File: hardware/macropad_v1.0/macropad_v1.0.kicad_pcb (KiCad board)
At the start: 2 copper layers, 66.7 x 81 mm, 51 parts, among them J1 USB_C_Receptacle_USB2.0_14P, SW1 SW_Push, SW2 Rotary Encoder, SW3 Rotary Encoder, U1 USBLC6-2SC6, U2 STM32F072C8T6, U3 XC6206PxxxMR

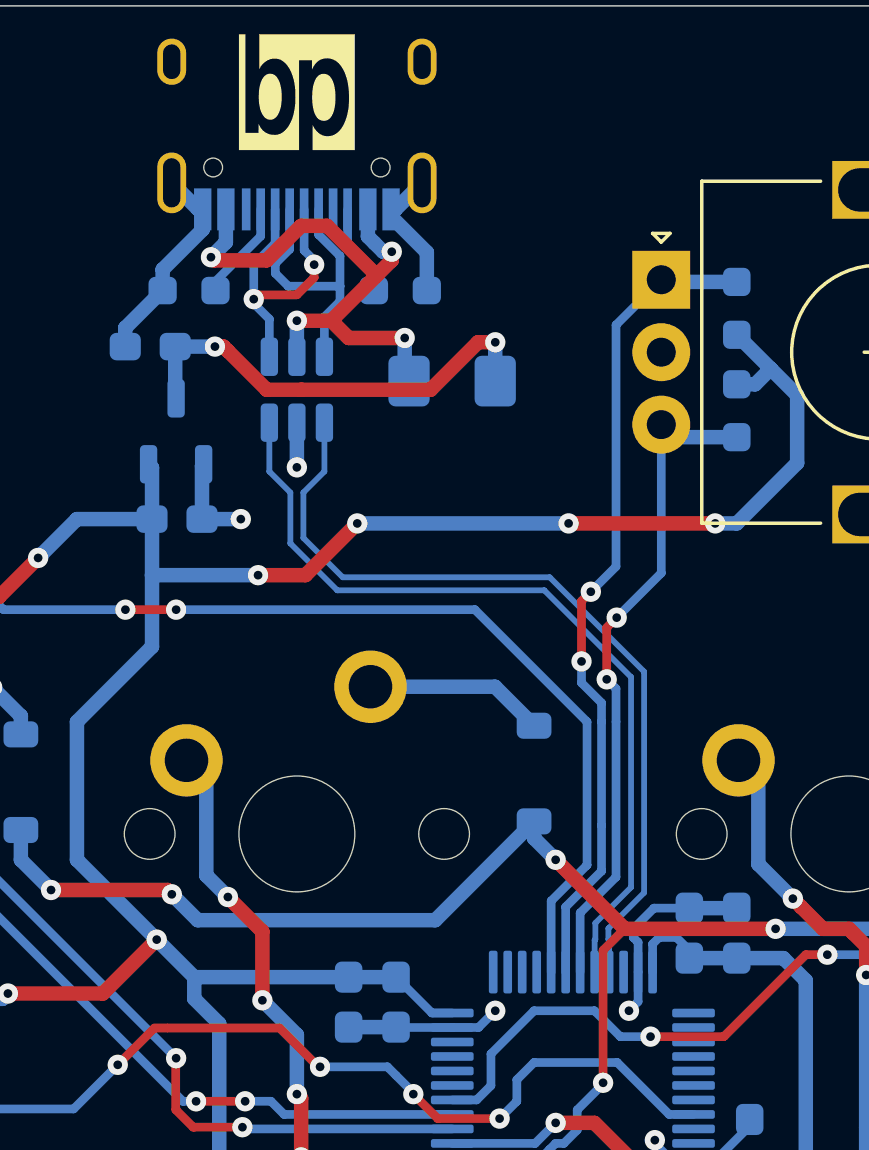
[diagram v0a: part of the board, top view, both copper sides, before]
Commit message: Changed USB-C routing
-Changed routing from usb-c module to esd protection module by shorting the pair of D+ and D- pins. New routing doesn't use a via, has shorter traces from usb module to esd module, and matches the length of the traces for D+ and D- better than the previous design did.

-Increased the width of the differential pair data traces from esd module to mcu from 0.2mm to 0.3mm to match traces that go into the esd module. Kicad made them 0.2mm by default for some reason.

-Next steps: change the routing near the MCU to eliminate overuse of vias, add a ground plane to the bottom layer and add stitching vias to connect the two planes
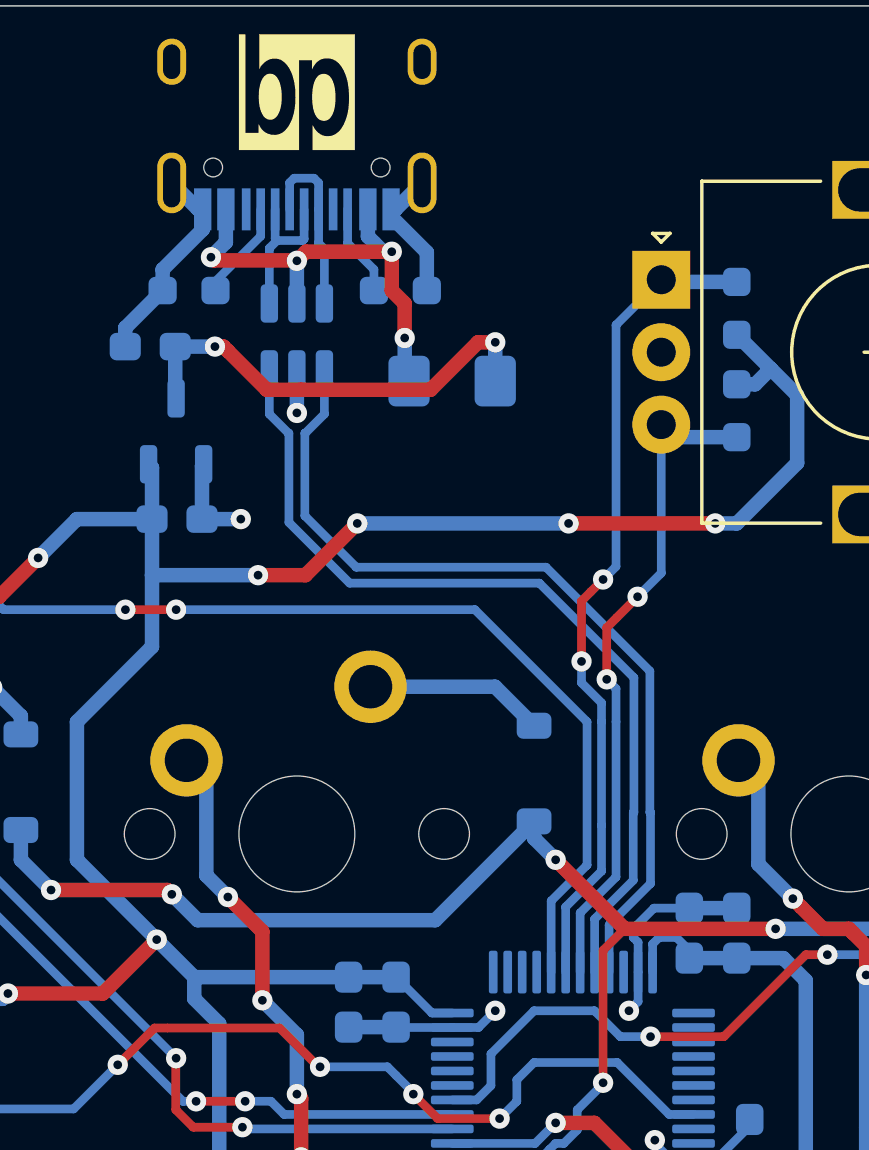
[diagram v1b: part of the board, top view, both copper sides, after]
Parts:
- moved U1 1.84 mm to (200.0, 30.5)
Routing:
- net ESD_D-: track 10.5 -> 5.37 mm, vias 2 -> 0
- net VBUS: track 20.8 -> 16.4 mm
- net ESD_D+: track 10.4 -> 6.30 mm
- net USB_D+: track 28.8 -> 30.5 mm
- net USB_D-: track 28.8 -> 30.4 mm

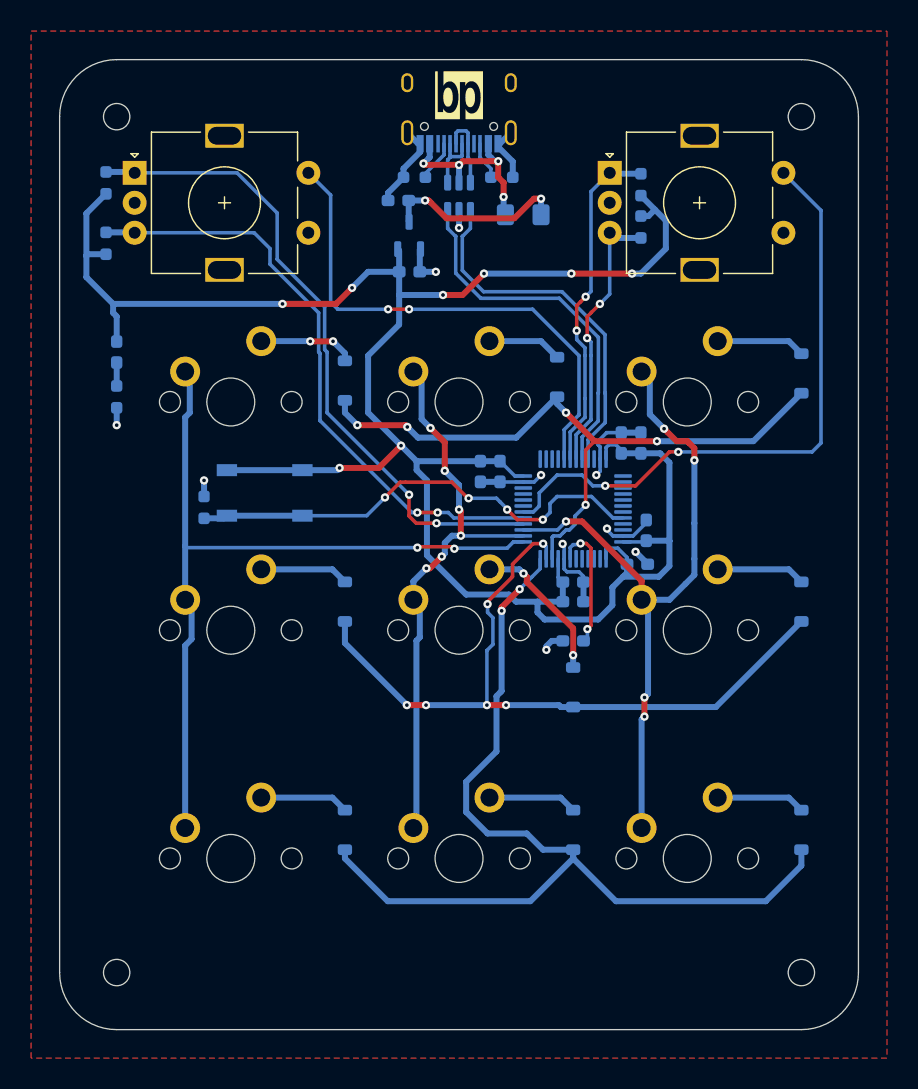
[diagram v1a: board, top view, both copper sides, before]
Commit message: Changed routing
-Edited traces to avoid overusing vias

-Next steps: Add stitching vias to connect the two ground planes
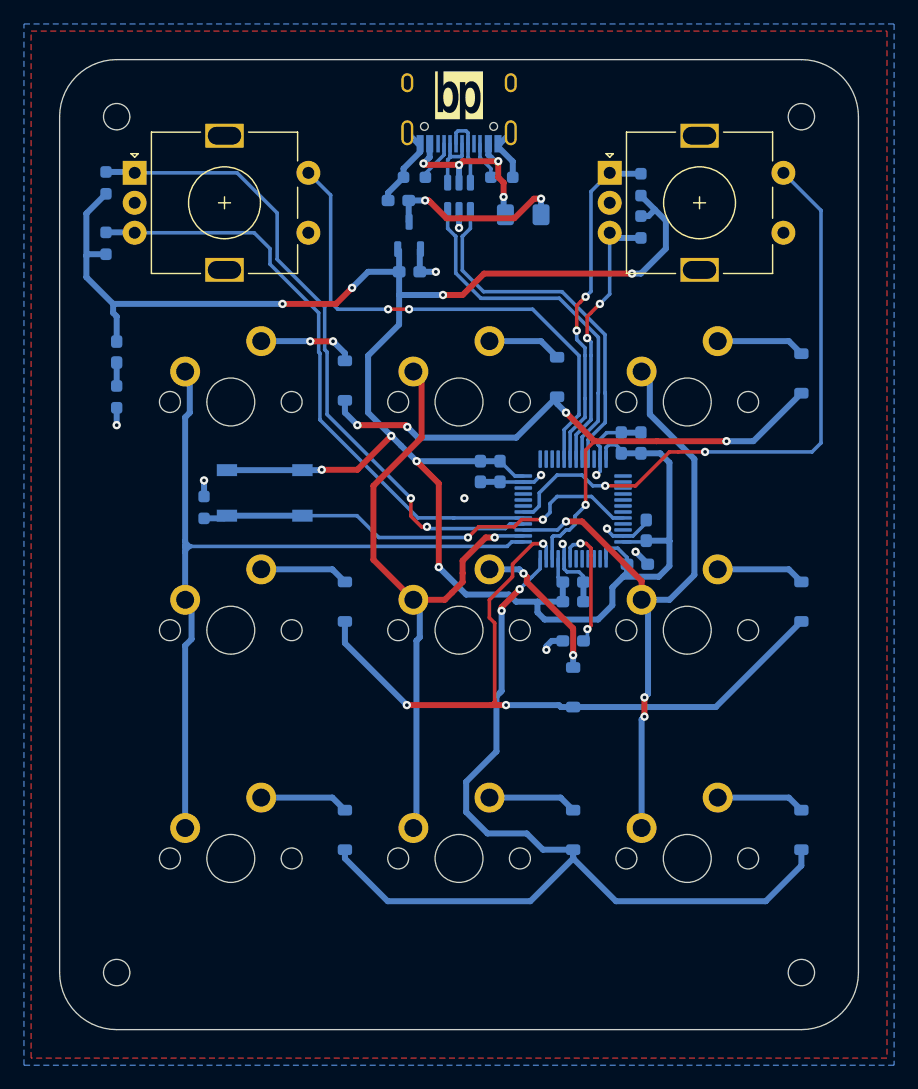
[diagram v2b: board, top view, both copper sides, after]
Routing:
- net COL_1: track 47.7 -> 54.3 mm, vias 6 -> 1
- net COL_0: track 67.5 -> 68.7 mm, vias 2 -> 0
- net BOOT0: track 39.5 -> 38.4 mm, vias 4 -> 2
- net ROW_1: track 62.7 -> 63.5 mm, vias 6 -> 3
- net COL_2: track 57.9 -> 57.4 mm, vias 5 -> 3
- net RENC_B1: track 50.7 -> 50.6 mm, vias 2 -> 0
- net GND: vias 10 -> 11
- added copper zone on B.Cu, net GND

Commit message: Added stitching vias
-Next steps: upload files to jlcpcb, generate a bom, figure out what I'm going to hand-solder, and order everything
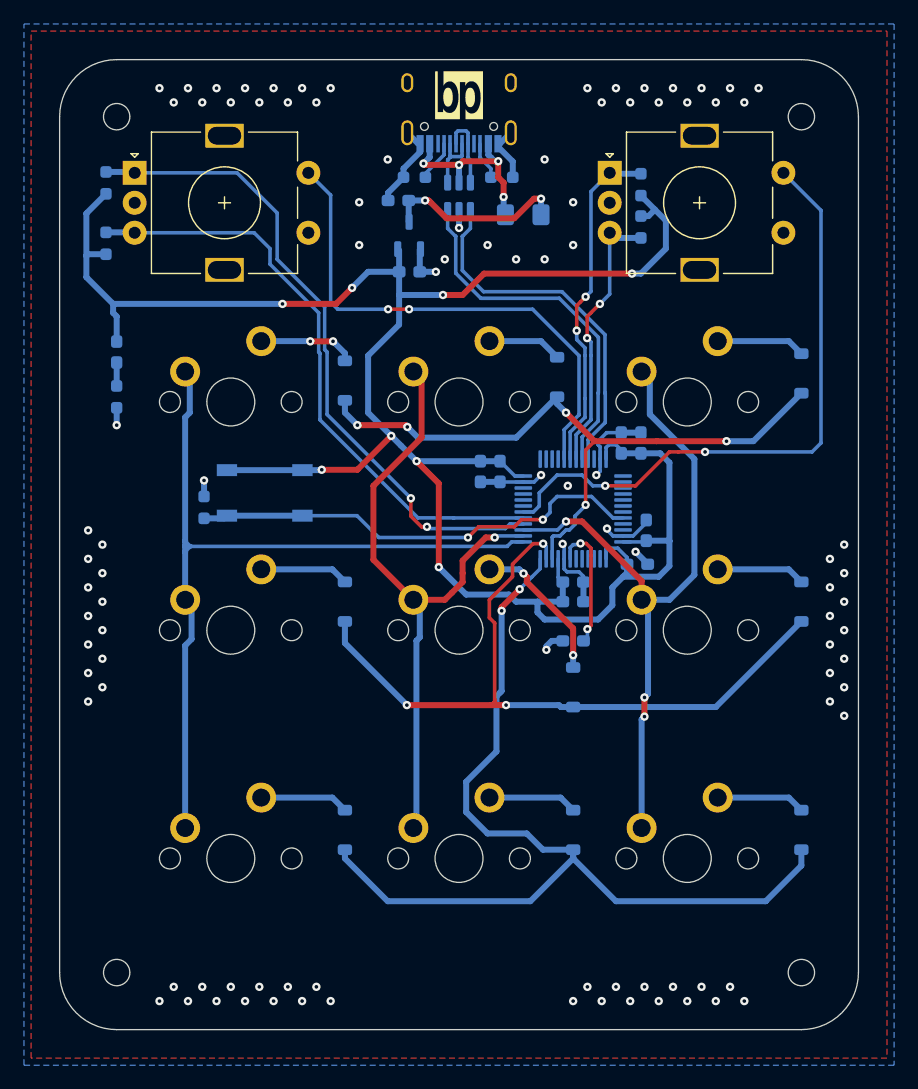
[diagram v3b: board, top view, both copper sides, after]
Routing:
- net GND: vias 11 -> 99

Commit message: Updated silkscreen and naming stuff, added keepouts
-Added ParPad logo to fron silkscreen

-Changed the name of the design in the little design box in the bottom right of the pcb and schematic

-Added two keepout zones to certain areas of the bottom ground fill to avoid an error about thermal spokes (only had one spoke, just got rid of the spoke cuz the top ground layer already has four spokes), and also a warning about some copper thing being too narrow
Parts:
- added G***: LOGO, LOGO, F.Cu at (200.0, 96.4)
- G***: moved to B.Cu
- turned G*** to 180 degrees

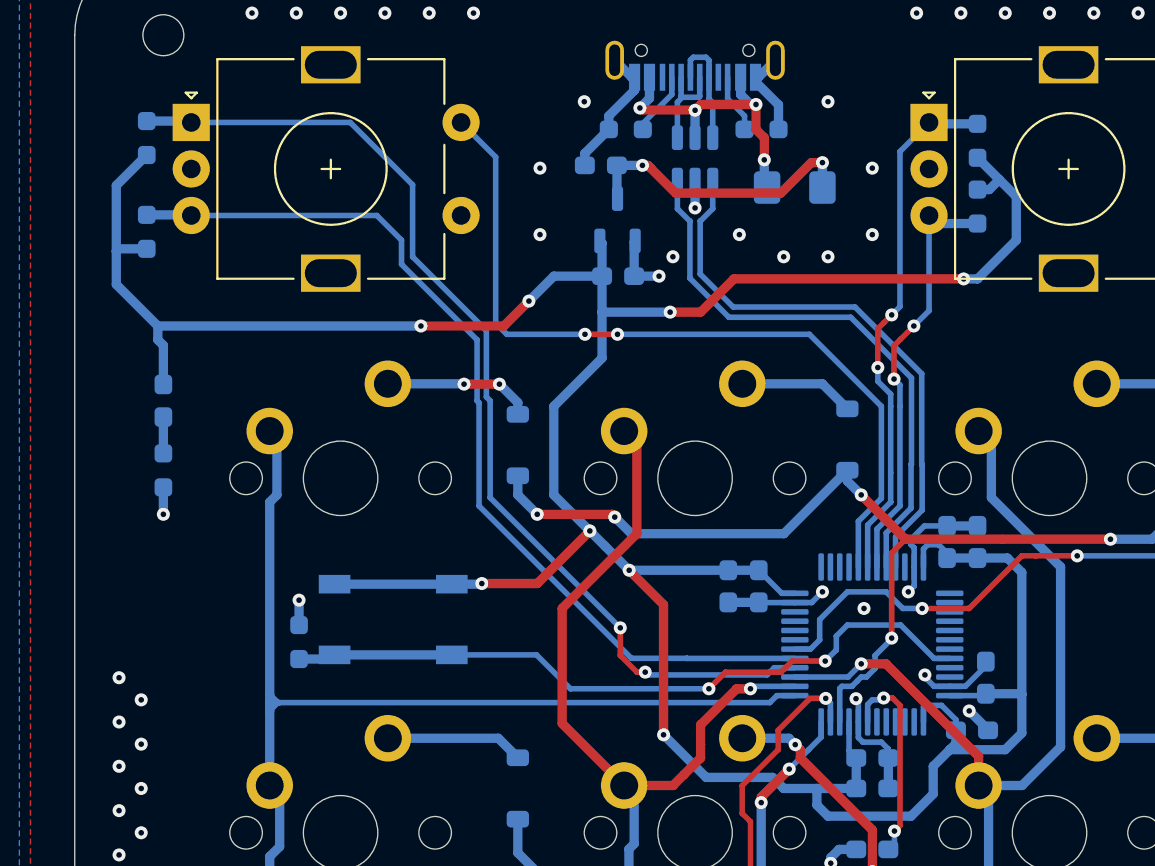
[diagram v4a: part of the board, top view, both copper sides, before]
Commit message: Updated stuff according to jlcpcb specifications and added production files
-Moved the resistors connected to the rotary encoder pins to be further away cuz jlcpcb was mad about tht to smd pad clearance

-added some more keepouts to bottom gnd plane to get rid of some drc errors about thermal spokes and stuff

-Moved a via near one of the encoders cuz it was overlapping the silkscreen

-Moved a couple designators cuz they overlapped with vias

-Moved C1 (decoupling cap) cuz it was too close to one of the through holes for the switch pins

-Changed bottom silkscreen to say ParPad instead of PARpad

-Added production files (bom, placements, gerbers, etc. idrk what else is in there tbh)
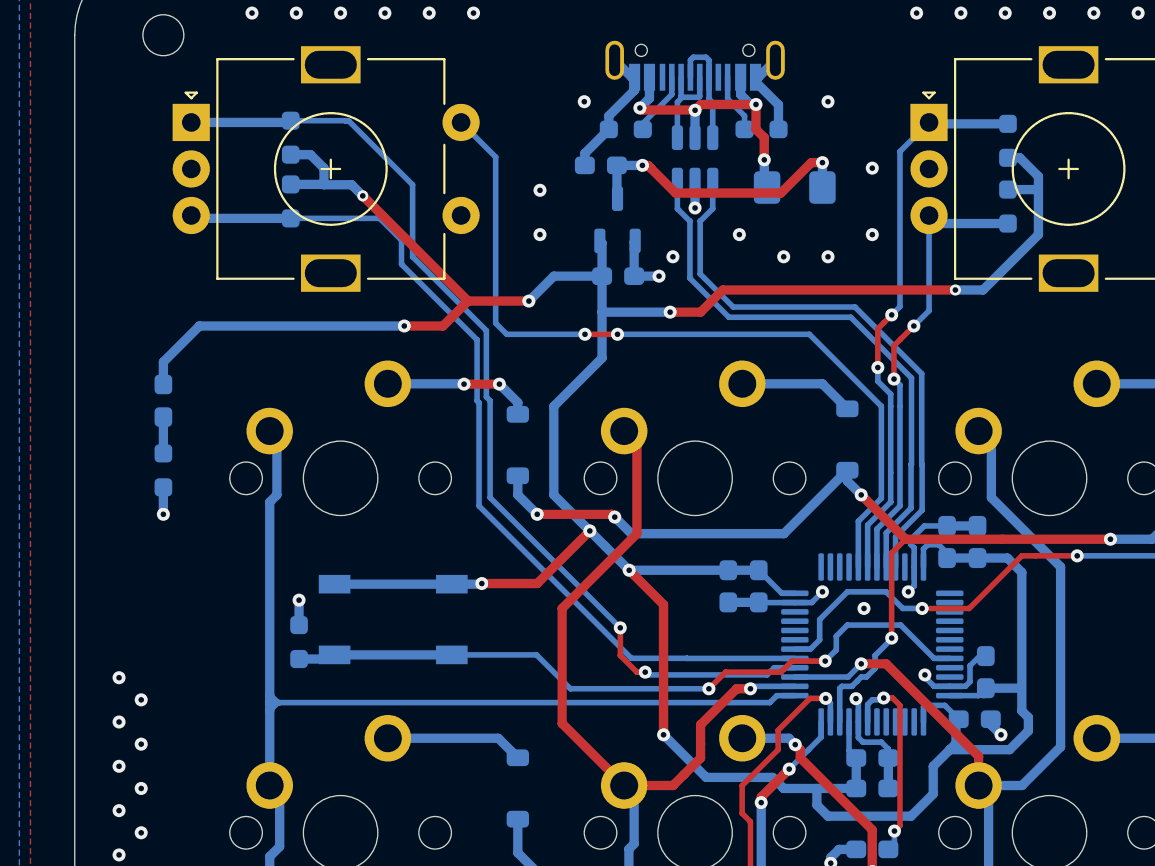
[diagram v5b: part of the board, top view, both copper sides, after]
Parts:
- moved R6 7.91 mm to (178.3, 32.7), turned to -90 degrees
- moved R5 7.74 mm to (178.3, 29.3)
- moved R7 1.64 mm to (216.8, 29.5)
- moved R8 1.64 mm to (216.8, 33.0)
- moved C1 0.61 mm to (215.1, 60.6)
- moved C5 0.30 mm to (215.7, 58.0)
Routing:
- net VBAT: track 180.2 -> 183.6 mm, vias 8 -> 9
- net RENC_B1: track 50.6 -> 48.3 mm
- net RENC_A1: track 55.6 -> 53.4 mm
- net RENC_B2: track 23.1 -> 24.7 mm
- net RENC_A2: track 28.5 -> 30.1 mm
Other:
- board text added: "ParPad v1.0"
- board text removed: "PARpad v1.0"
